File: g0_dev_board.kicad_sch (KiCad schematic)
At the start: 0 parts

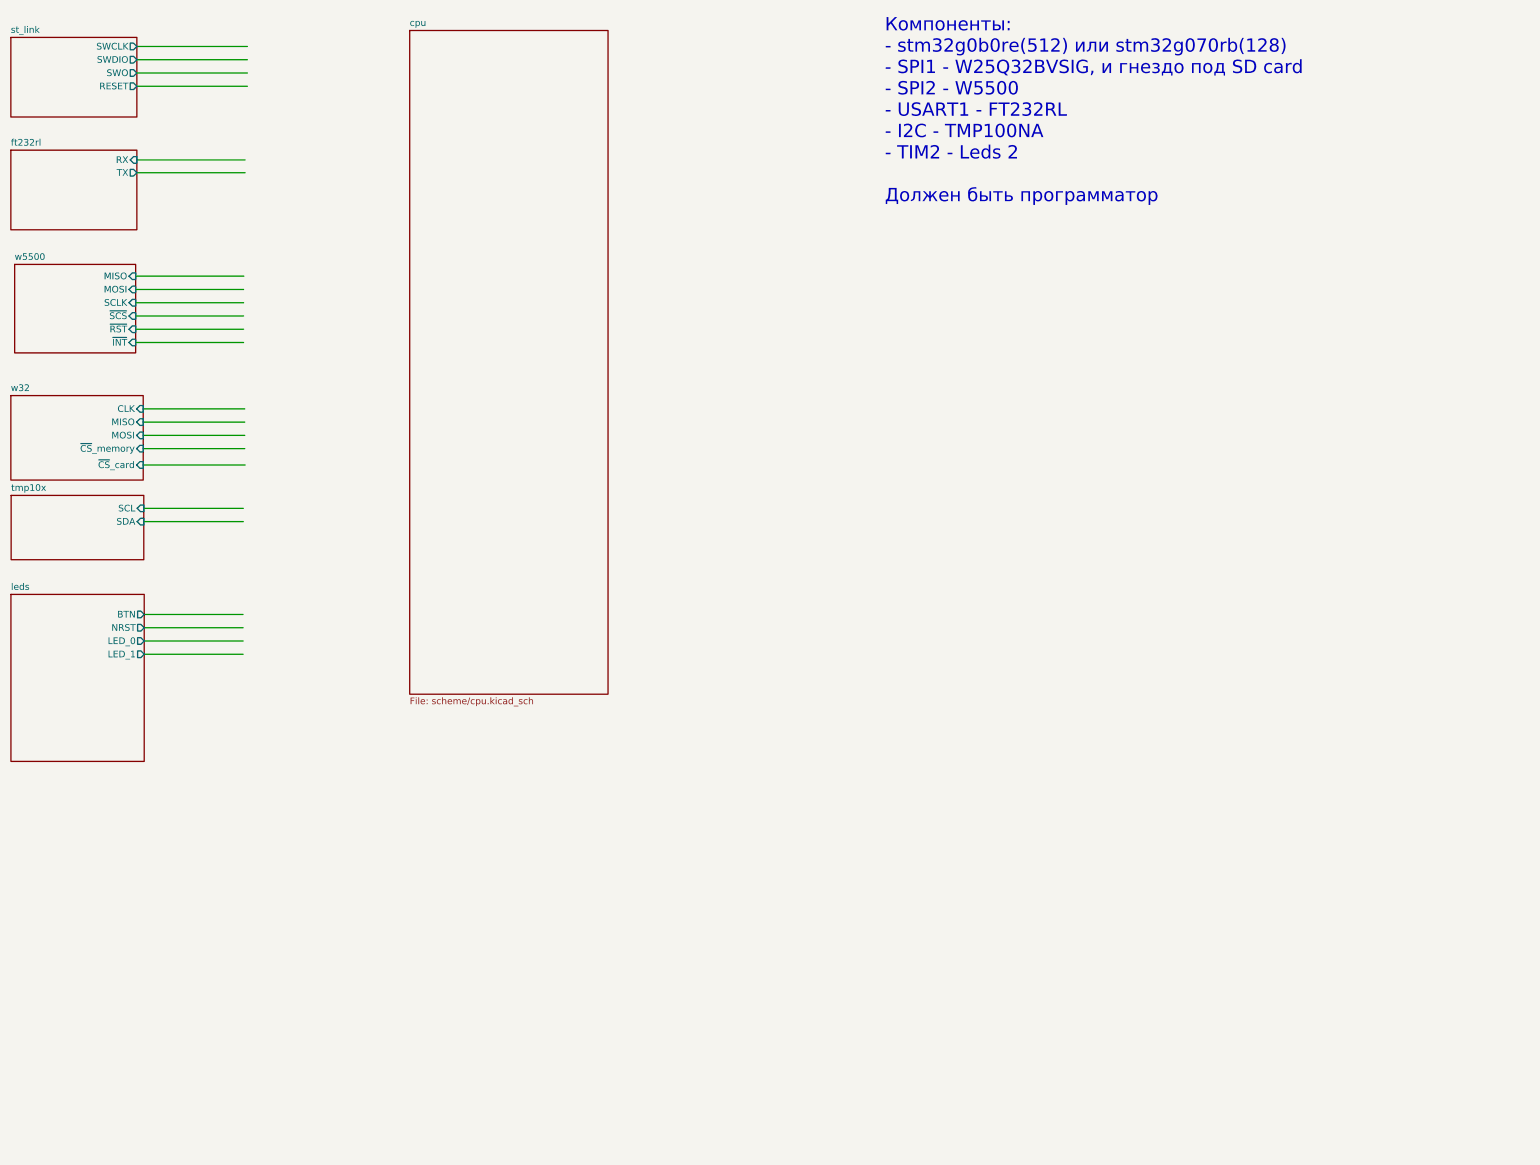
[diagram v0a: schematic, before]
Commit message: feat(schematic): fix peripheral sheets and integrate STM32G0B1CCT6
Главный МК заменён на STM32G0B1CCT6 (LQFP-48, pin-to-pin совместим
с STM32G071CBT6). Лист cpu переписан: обвязка по DS13560, LSE
32.768 кГц, подстроечник на ADC (PA4), перемычка JP_IDD, таблица
назначения выводов.

Исправлены листы периферии:
- st_link: перепутанные USB D+/D-, закороченные резисторы SWD,
  VBUS через PTC и Шоттки, ESD USBLC6-2SC6, LDO AP7361C-33E,
  SWO стянут на землю, J2 1x5 с NRST, перемычка JP_STL_PWR;
- ft232rl: 3V3OUT отвязан от общей шины +3.3V, разделены цепи
  TX/RX и светодиодов, ESD, Шоттки на VBUS, делитель на RESET#;
- w5500: номиналы терминации MDI (49.9 Ом / 10 Ом), PMODE=111,
  RSVD на GND, бусина аналогового питания, подтяжки RST/SCS/INT;
- w32: флэш W25Q32JVSSIQ, символ microSD с детектом карты,
  подтяжки линий SD;
- tmp10x: подтяжки I2C, адреса без резисторов, развязка 100 нФ.

Добавлен лист headers: разъёмы Arduino Uno R3 без ICSP, гребёнки
логического анализатора 1x27 с двух сторон, перемычки JP_SWD.
Удалён пустой лист memory. ERC: 0 ошибок.
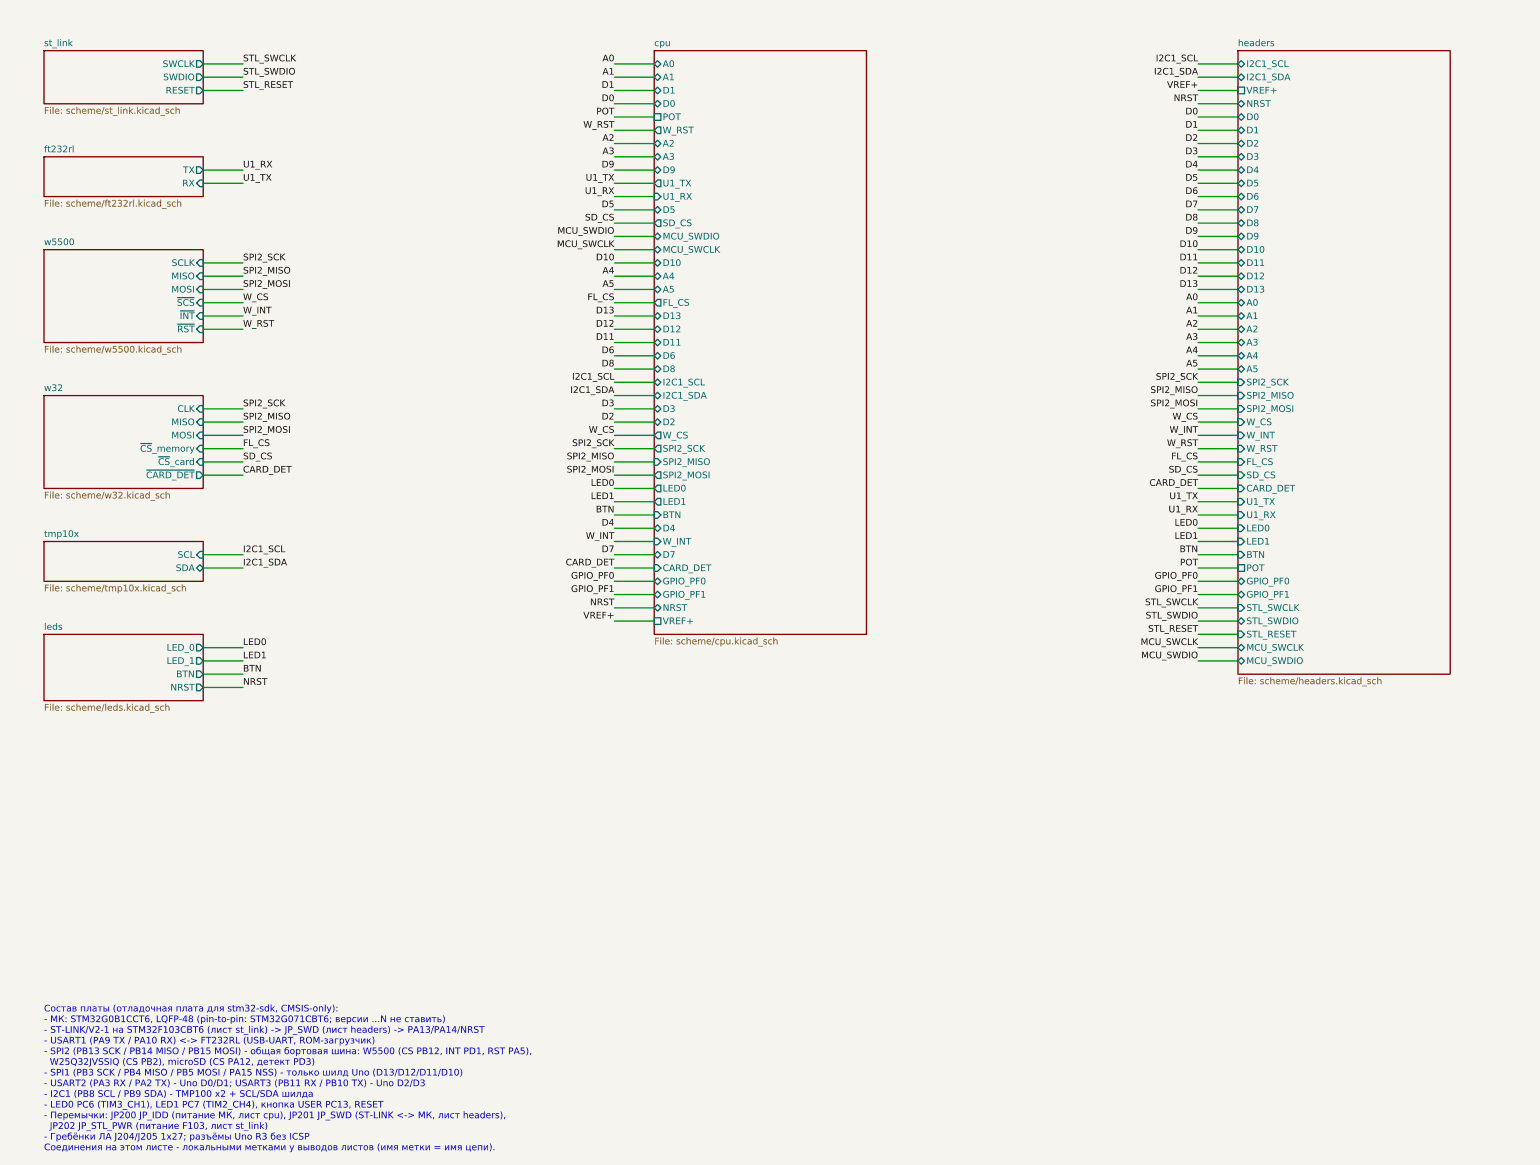
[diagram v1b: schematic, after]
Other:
- added sheet headers (scheme/headers.kicad_sch)
- sheet cpu ports: added A0, A1, A2, A3, A4, A5, BTN, CARD_DET, D0, D1, D10, D11, D12, D13, D2, D3, D4, D5, D6, D7, D8, D9, FL_CS, GPIO_PF0, GPIO_PF1, I2C1_SCL, I2C1_SDA, LED0, LED1, MCU_SWCLK, MCU_SWDIO, NRST, POT, SD_CS, SPI2_MISO, SPI2_MOSI, SPI2_SCK, U1_RX, U1_TX, VREF+, W_CS, W_INT, W_RST; removed none
- sheet st_link ports: added none; removed SWO
- sheet w32 ports: added ~{CARD_DET}; removed none
- note added: "Состав платы (отладочная плата для stm32-sdk, CMSIS-only): - МК: STM32G0B1CCT6, LQFP-48 (pin-to-pin: STM32G071CBT6; версии ...N не ставить) - ST-LINK/V2-1 на STM32F103CBT6 (лист st_link) -> JP_SWD (лист headers) -> PA13/PA14/NRST - USART1 (PA9 TX / PA10 RX) <-> FT232RL (USB-UART, ROM-загрузчик) - SPI2 (PB13 SCK / PB14 MISO / PB15 MOSI) - общая бортовая шина: W5500 (CS PB12, INT PD1, RST PA5), W25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"
- note removed: "Компоненты: - stm32g0b0re(512) или stm32g070rb(128) - SPI1 - W25Q32BVSIG, и гнездо под SD card - SPI2 - W5500 - USART1 - FT232RL - I2C - TMP100NA - TIM2 - Leds 2 Должен быть программатор"
- title: (none) -> G0 dev board
